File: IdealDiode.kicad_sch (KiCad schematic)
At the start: 5 parts, among them Q1 FDMT800100DC, U1 LTC4357DCB

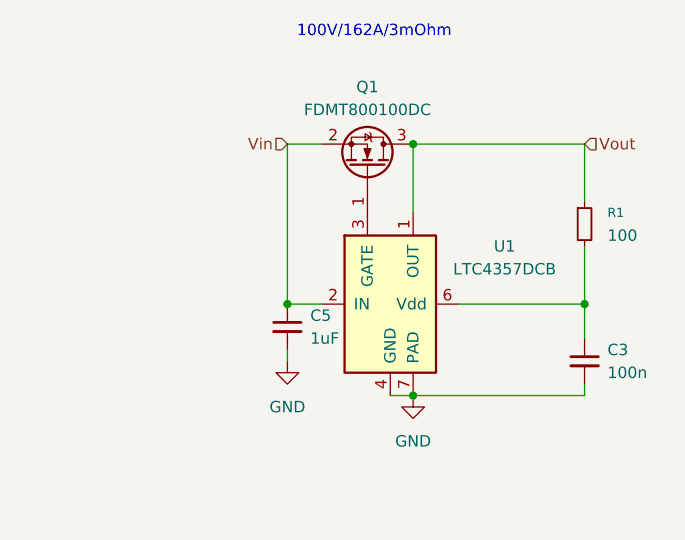
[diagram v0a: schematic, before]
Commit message: skiftet til LTC4359
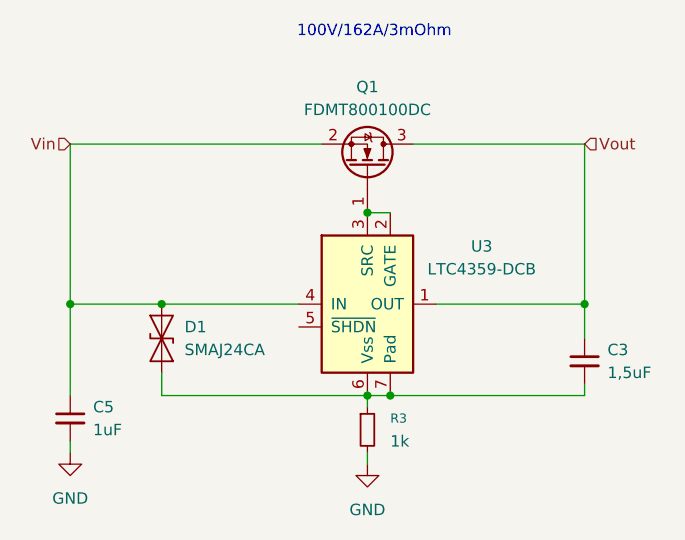
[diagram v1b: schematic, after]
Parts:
- removed R1: 100, Resistor_SMD:R_0603_1608Metric, symbol Device:R_Small
- removed U1: LTC4357DCB, Package_DFN_QFN:DFN-6-1EP_3x2mm_P0.5mm_EP1.65x1.35mm, symbol Power_Management:LTC4357DCB
- added D1: SMAJ24CA, Diode_SMD:D_SMA, symbol Diode:SMAJ24CA
- added R3: 1k, Resistor_SMD:R_0603_1608Metric, symbol Device:R_Small
- added U3: LTC4359-DCB, Package_DFN_QFN:DFN-6-1EP_3x2mm_P0.5mm_EP1.65x1.35mm, symbol Power_Management:LTC4359-DCB
- C3: value 100n -> 1,5uF
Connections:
- net GND: now also R3.2; no longer C3.2
- net Vin: now also D1.2 (A2), U3.4 (IN)
- net Vout: now also C3.1, U3.1 (OUT)
- net at Q1.1 (G): now also U3.2 (GATE), U3.3 (SRC)
- new net: C3.2, D1.1 (A1), R3.1, U3.6 (Vss), U3.7 (Pad)
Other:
- moved on the sheet: C5

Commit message: fejlretning
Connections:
- net Vin: now also U3.3 (SRC)
- net at Q1.1 (G), U3.2 (GATE): no longer U3.3 (SRC)
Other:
- moved on the sheet: Q1
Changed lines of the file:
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@@
+	)
+	(junction
+		(at 121.92 82.55)
+		(diameter 0)
+		(color 0 0 0 0)
 	)
 	(junction
@@
 	)
 	(junction
-		(at 124.46 90.17)
-		(diameter 0)
-		(color 0 0 0 0)
-	)
-	(junction
 		(at 127 110.49)
 		(diameter 0)
@@
 	(wire
 		(pts
-			(xy 124.46 90.17) (xy 127 90.17)
-		)
-		(stroke
-			(width 0)
-			(type default)
-		)
-	)
-	(wire
-		(pts
 			(xy 91.44 110.49) (xy 91.44 100.33)
 		)
@@
 	(wire
 		(pts
+			(xy 124.46 90.17) (xy 121.92 90.17)
+		)
+		(stroke
+			(width 0)
+			(type default)
+		)
+	)
+	(wire
+		(pts
 			(xy 124.46 110.49) (xy 124.46 111.76)
 		)
@@
 	(wire
 		(pts
-			(xy 129.54 82.55) (xy 148.59 82.55)
+			(xy 132.08 82.55) (xy 148.59 82.55)
 		)
 		(stroke
@@
 	(wire
 		(pts
+			(xy 121.92 90.17) (xy 121.92 82.55)
+		)
+		(stroke
+			(width 0)
+			(type default)
+		)
+	)
+	(wire
+		(pts
 			(xy 91.44 100.33) (xy 91.44 82.55)
 		)
@@
 	(wire
 		(pts
-			(xy 91.44 82.55) (xy 119.38 82.55)
+			(xy 91.44 82.55) (xy 121.92 82.55)
 		)
 		(stroke
@@
 	(symbol
 		(lib_id "Transistor_FET:FDMT800100DC")
-		(at 124.46 85.09 270)
+		(at 127 85.09 270)
 		(mirror x)
 		(unit 1)
@@
 		(fields_autoplaced yes)
 		(property "Reference" "Q1"
-			(at 124.46 76.2 90)
+			(at 127 76.2 90)
 			(effects
 				(font
@@
 		)
 		(property "Value" "FDMT800100DC"
-			(at 124.46 78.74 90)
+			(at 127 78.74 90)
 			(effects
 				(font
@@
 		)
 		(property "Footprint" "Package_TO_SOT_SMD:PQFN_8x8"
-			(at 122.555 80.01 0)
+			(at 125.095 80.01 0)
 			(effects
 				(font
@@
 		)
 		(property "Datasheet" "https://www.onsemi.com/pub/Collateral/FDMT800100DC-D.pdf"
-			(at 120.65 80.01 0)
+			(at 123.19 80.01 0)
 			(effects
 				(font
@@
 		)
 		(property "Description" "24A Id, 100V Vds, N-Channel Dual Cool PowerTrench MOSFET, 2.95mOhm Ron, 111nC Qgmax, -55 to 150 °C, 8x8mm MLP"
-			(at 124.46 85.09 0)
-			(effects
-				(font
+			(at 127 85.09 0)
+			(effects
+				(font
